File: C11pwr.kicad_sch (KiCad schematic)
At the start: 45 parts, among them IC1 MPM3610AGQV-P, IC6 MAX17613AATP+, IC8 MAX17613AATP+, J8 Screw_Terminal_01x02, U5 L78M12

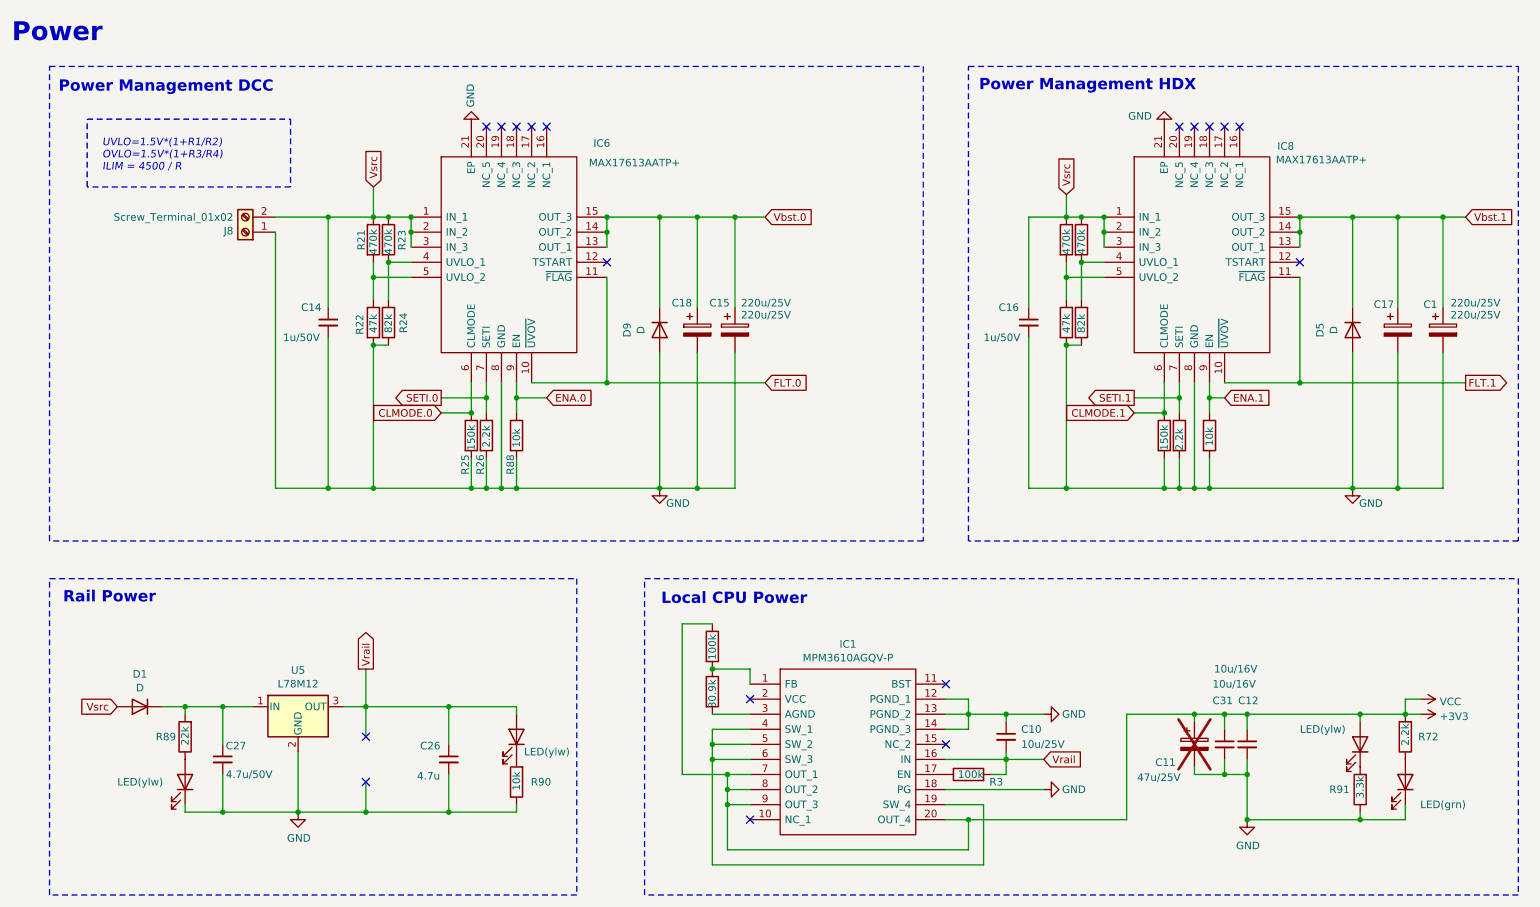
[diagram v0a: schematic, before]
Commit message: mod: changed to buck converter
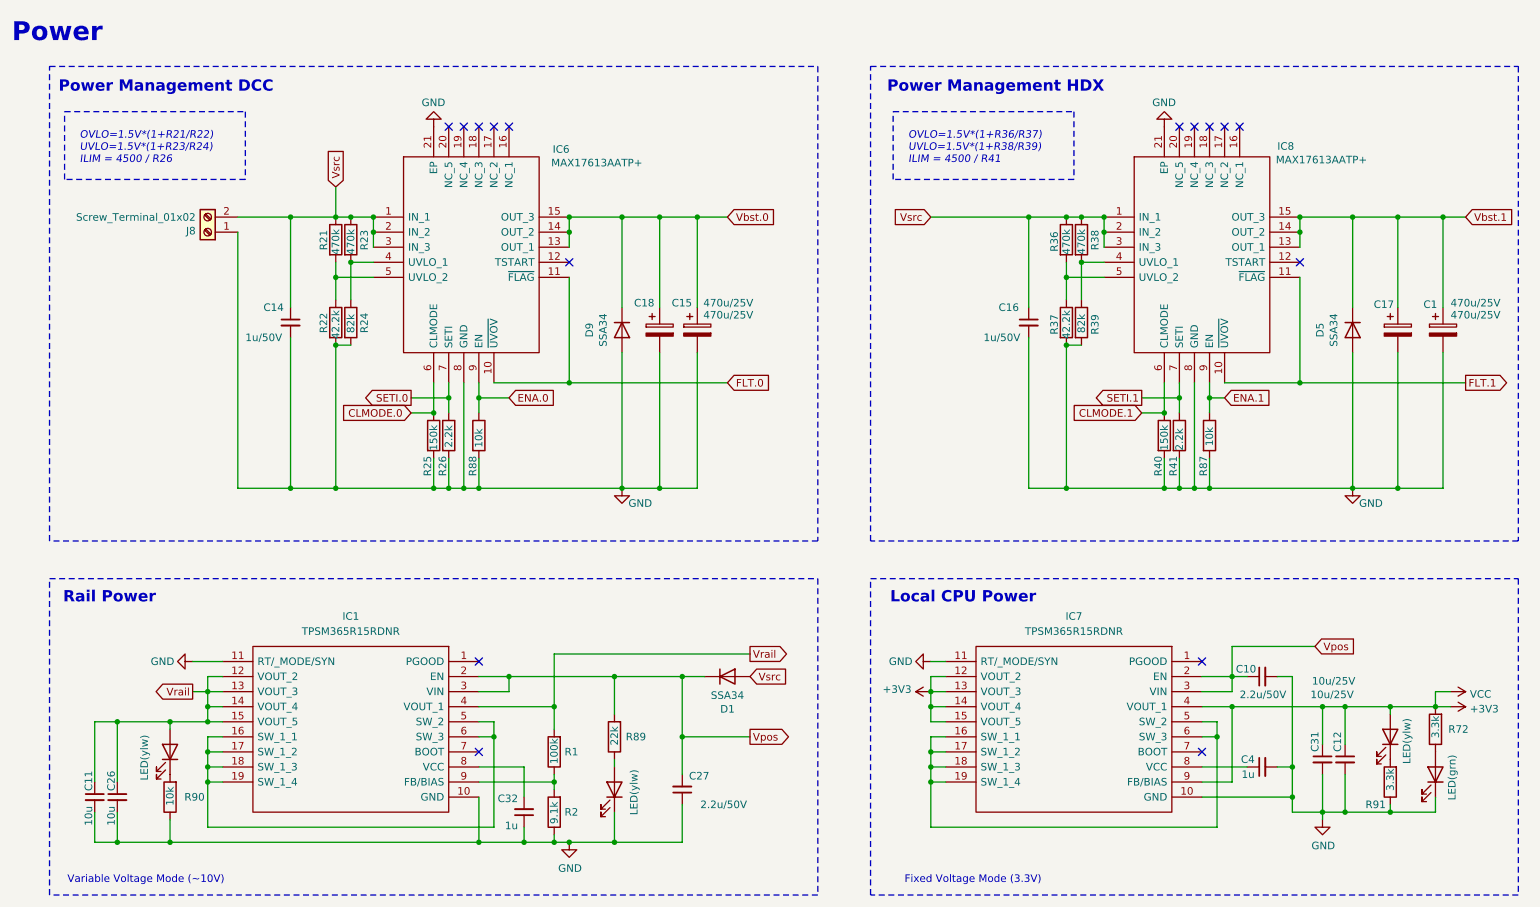
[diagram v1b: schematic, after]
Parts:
- removed C11: 47u/25V, Capacitor_Tantalum_SMD:CP_EIA-7343-31_Kemet-D, symbol Device:CP
- removed IC1: MPM3610AGQV-P, MPM3610AGQVP, symbol RTB:MPM3610AGQV-P
- removed R3: 100k, Resistor_SMD:R_0402_1005Metric, symbol Device:R
- removed U5: L78M12, Package_TO_SOT_SMD:TO-252-2, symbol Regulator_Linear:L7812
- added C11: 10u, Capacitor_SMD:C_1206_3216Metric, symbol Device:C_Small
- added C32, C4: 1u, Capacitor_SMD:C_0402_1005Metric, symbol Device:C_Small
- added IC1, IC7: TPSM365R15RDNR, TPSM365R3RDNR, symbol RTB:TPSM365R1FRDNR
- C1, C15, C17, C18: value 220u/25V -> 470u/25V; now left out of the parts list
- C10: value 10u/25V -> 2.2u/50V; footprint Capacitor_SMD:C_0805_2012Metric -> Capacitor_SMD:C_1206_3216Metric; LCSC Part # (none) -> C50254
- C12, C31: value 10u/16V -> 10u/25V; LCSC Part # (none) -> C96446
- C14, C16: LCSC Part # (none) -> C28323
- C26: value 4.7u -> 10u; LCSC Part # (none) -> C694197
- C27: value 4.7u/50V -> 2.2u/50V; LCSC Part # (none) -> C50254
- D1, D5, D9: value D -> SSA34; LCSC Part # (none) -> C84632
- D14, D2, D25, D26, J8: now left out of the parts list
- IC6, IC8: Height 0.8 -> (none); LCSC Part # (none) -> C3198161; Manufacturer_Name Maxim Integrated -> (none); Manufacturer_Part_Number MAX17613AATP+ -> (none); Mouser Part Number 700-MAX17613AATP+ -> (none); Mouser Price/Stock https://www.mouser.co.uk/ProductDetail/Maxim-Integrated/MAX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 -> (none)
- R1: LCSC Part # (none) -> C25741
- R2: value 30.9k -> 9.1k; LCSC Part # (none) -> C25926
- R21, R23, R36, R38: LCSC Part # (none) -> C23178
- R22, R37: value 47k -> 42.2k; LCSC Part # (none) -> C23167
- R24, R39: LCSC Part # (none) -> C23254
- R25, R40: LCSC Part # (none) -> C22807
- R26, R41: LCSC Part # (none) -> C4190
- R72: value 2.2k -> 3.3k; LCSC Part # (none) -> C22978
- R87: LCSC Part # (none) -> C25744
- R88, R90: LCSC Part # (none) -> C25804
- R89: LCSC Part # (none) -> C31850
- R91: LCSC Part # (none) -> C22978
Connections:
- net +3V3: now also IC7.12 (VOUT_2), IC7.13 (VOUT_3), IC7.14 (VOUT_4), IC7.15 (VOUT_5), IC7.4 (VOUT_1), IC7.9 (FB/BIAS); no longer R1.1
- net GND: now also C10.2, C27.1, R2.1, C11.2, C32.1, C4.2, IC1.10 (GND), IC1.11 (RT/_MODE/SYN), IC7.10 (GND), IC7.11 (RT/_MODE/SYN); no longer C10.1, C27.2
- net Vrail: now also R1.2, C11.1, IC1.12 (VOUT_2), IC1.13 (VOUT_3), IC1.14 (VOUT_4), IC1.15 (VOUT_5), IC1.4 (VOUT_1); no longer C10.2
- net Vpos: now reaches D1.1 (K), R89.2
- net Vpos: now also C10.1, C27.2, IC1.2 (EN), IC1.3 (VIN), IC7.2 (EN), IC7.3 (VIN); no longer C27.1
- net at R2.2: now also R1.1, IC1.9 (FB/BIAS)
- new net: IC1.16 (SW_1_1), IC1.17 (SW_1_2), IC1.18 (SW_1_3), IC1.19 (SW_1_4), IC1.5 (SW_2), IC1.6 (SW_3)
- new net: C32.2, IC1.8 (VCC)
- new net: IC7.16 (SW_1_1), IC7.17 (SW_1_2), IC7.18 (SW_1_3), IC7.19 (SW_1_4), IC7.5 (SW_2), IC7.6 (SW_3)
- new net: C4.1, IC7.8 (VCC)
- no-connect marks 18 -> 16
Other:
- note added: "Fixed Voltage Mode (3.3V)"
- note added: "OVLO=1.5V*(1+R21/R22) UVLO=1.5V*(1+R23/R24) ILIM = 4500 / R26"
- note added: "OVLO=1.5V*(1+R36/R37) UVLO=1.5V*(1+R38/R39) ILIM = 4500 / R41"
- note added: "Variable Voltage Mode (~10V)"
- note removed: "UVLO=1.5V*(1+R1/R2) OVLO=1.5V*(1+R3/R4) ILIM = 4500 / R"
- moved on the sheet: C10, C12, C14, C15, C18, C26, C27, C31, D1, D9, IC6, J8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
